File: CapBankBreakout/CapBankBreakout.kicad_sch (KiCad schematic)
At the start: 32 parts

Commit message: commit 2
hi brady
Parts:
- added J1, J2: 7461097, 7461097, symbol KineticAntenna:7461097
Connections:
- net PCB1_CAP+: now also J1.1, J1.10, J1.11, J1.12, J1.13, J1.14, J1.15, J1.16, J1.2, J1.3, J1.4, J1.5, J1.6, J1.7, J1.8, J1.9
- net PCB1_CAP-: now also J2.1, J2.10, J2.11, J2.12, J2.13, J2.14, J2.15, J2.16, J2.2, J2.3, J2.4, J2.5, J2.6, J2.7, J2.8, J2.9

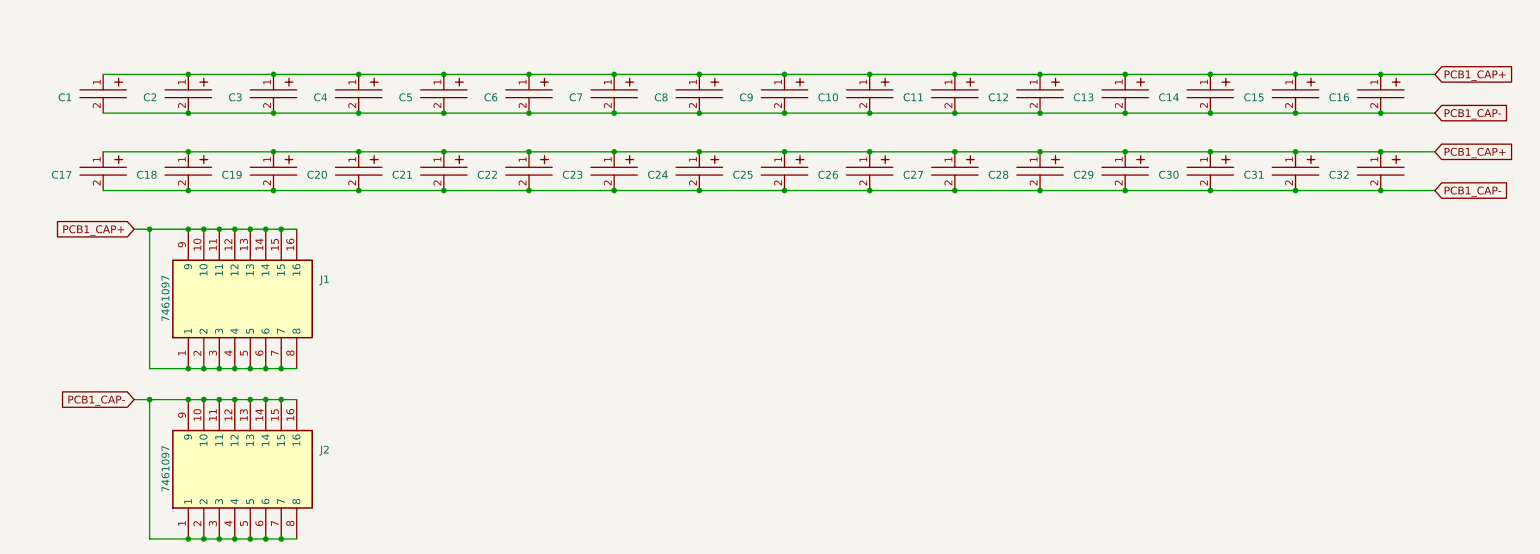
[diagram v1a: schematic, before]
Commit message: redesign 1
mouse bites inserted.
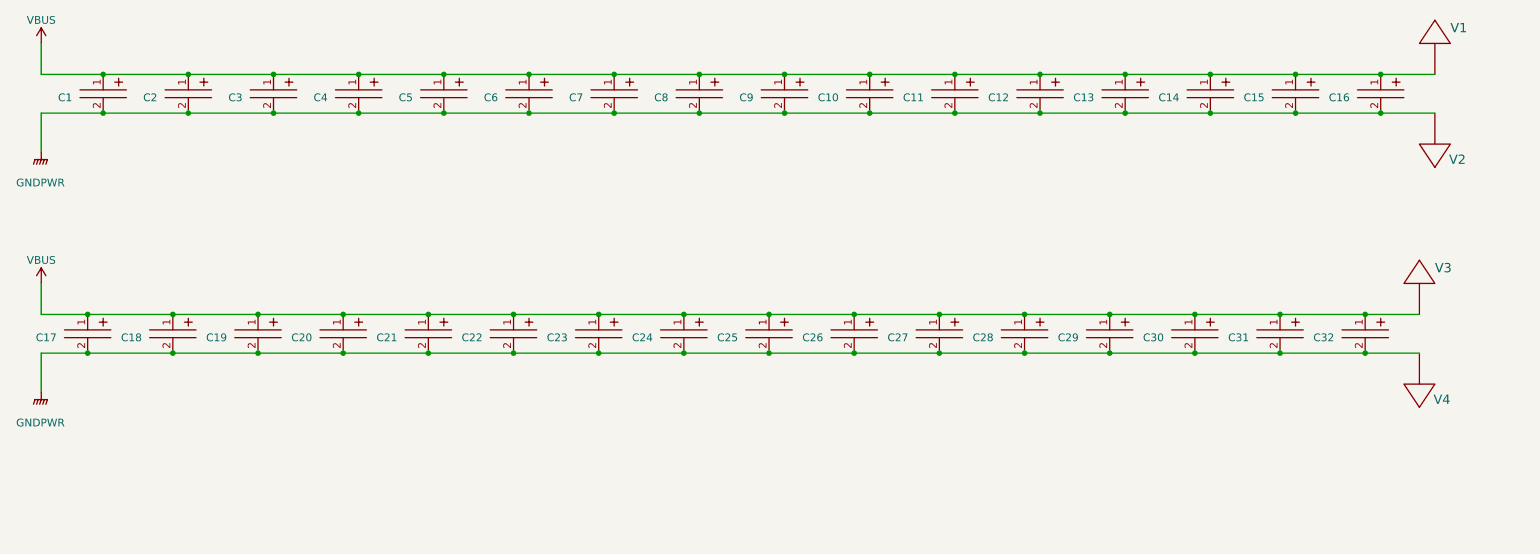
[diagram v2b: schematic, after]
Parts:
- removed J1, J2: 7461097, 7461097, symbol KineticAntenna:7461097
- added V1, V2, V3, V4: BATT_PWR_VIA, ALF70C103EH400:via, symbol MRDT_Drill_Holes:BATT_PWR_VIA
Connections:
- net PCB1_CAP+ renamed VBUS
- net VBUS: now also V1.1, V3.1
- net PCB1_CAP- renamed GNDPWR
- net GNDPWR: now also V2.1, V4.1
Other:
- moved on the sheet: C17, C18, C19, C20, C21, C22, C23, C24, C25, C26, C27, C28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
